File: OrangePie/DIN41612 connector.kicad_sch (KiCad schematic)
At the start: 0 parts

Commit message: Update rest of schematic
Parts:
- added J3: 09031967921, Connector_DIN:DIN41612_R_3x32_Female_Horizontal_THT, symbol DIN41612_3x32:09031967921
- added U10: IP4234CZ6,115, Package_TO_SOT_SMD:SC-74-6_1.55x2.9mm_P0.95mm, symbol Power_Protection:IP4234CZ6
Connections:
- new net 12V out: J3.a11, J3.a12, J3.b11, J3.b12, J3.c11, J3.c12
- new net 24v: J3.a14, J3.b14, J3.c14
- new net CAN1.+: J3.a5
- new net CAN1.-: J3.a6
- new net CAN1..+: J3.b5, J3.c5
- new net CAN1..-: J3.b6, J3.c6
- new net CAN2.+: J3.a8
- new net CAN2.-: J3.a9
- new net CAN2..+: J3.b8, J3.c8
- new net CAN2..-: J3.b9, J3.c9
- new net GND: J3.a1, J3.a10, J3.a13, J3.a15, J3.a32, J3.a4, J3.a7, J3.b1, J3.b10, J3.b13, J3.b15, J3.b2, J3.b32, J3.b4, J3.b7, J3.c1, J3.c10, J3.c13, J3.c15, J3.c32, J3.c4, J3.c7, U10.2 (VN)
- new net GPIOC0: J3.b16
- new net GPIOC1: J3.b17
- new net GPIOC10: J3.b26
- new net GPIOC11: J3.b27
- new net GPIOC12: J3.b28
- new net GPIOC13: J3.b29
- new net GPIOC14: J3.b30
- new net GPIOC15: J3.b31
- new net GPIOC2: J3.b18
- new net GPIOC3: J3.b19
- new net GPIOC4: J3.b20
- new net GPIOC5: J3.b21
- new net GPIOC6: J3.b22
- new net GPIOC7: J3.b23
- new net GPIOC8: J3.b24
- new net GPIOC9: J3.b25
- new net GPIOL0: J3.a16
- new net GPIOL1: J3.a17
- new net GPIOL10: J3.a26
- new net GPIOL11: J3.a27
- new net GPIOL12: J3.a28
- new net GPIOL13: J3.a29
- new net GPIOL14: J3.a30
- new net GPIOL15: J3.a31
- new net GPIOL2: J3.a18
- new net GPIOL3: J3.a19
- new net GPIOL4: J3.a20
- new net GPIOL5: J3.a21
- new net GPIOL6: J3.a22
- new net GPIOL7: J3.a23
- new net GPIOL8: J3.a24
- new net GPIOL9: J3.a25
- new net GPIOR0: J3.c16
- new net GPIOR1: J3.c17
- new net GPIOR10: J3.c26
- new net GPIOR11: J3.c27
- new net GPIOR12: J3.c28
- new net GPIOR13: J3.c29
- new net GPIOR14: J3.c30
- new net GPIOR15: J3.c31
- new net GPIOR2: J3.c18
- new net GPIOR3: J3.c19
- new net GPIOR4: J3.c20
- new net GPIOR5: J3.c21
- new net GPIOR6: J3.c22
- new net GPIOR7: J3.c23
- new net GPIOR8: J3.c24
- new net GPIOR9: J3.c25
- new net STDBY OUT: J3.a3, J3.b3, J3.c3
- new net USB1U.D+: J3.a2, U10.4, U10.6
- new net USB1U.D-: J3.c2, U10.1, U10.3
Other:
- note added: "USB"

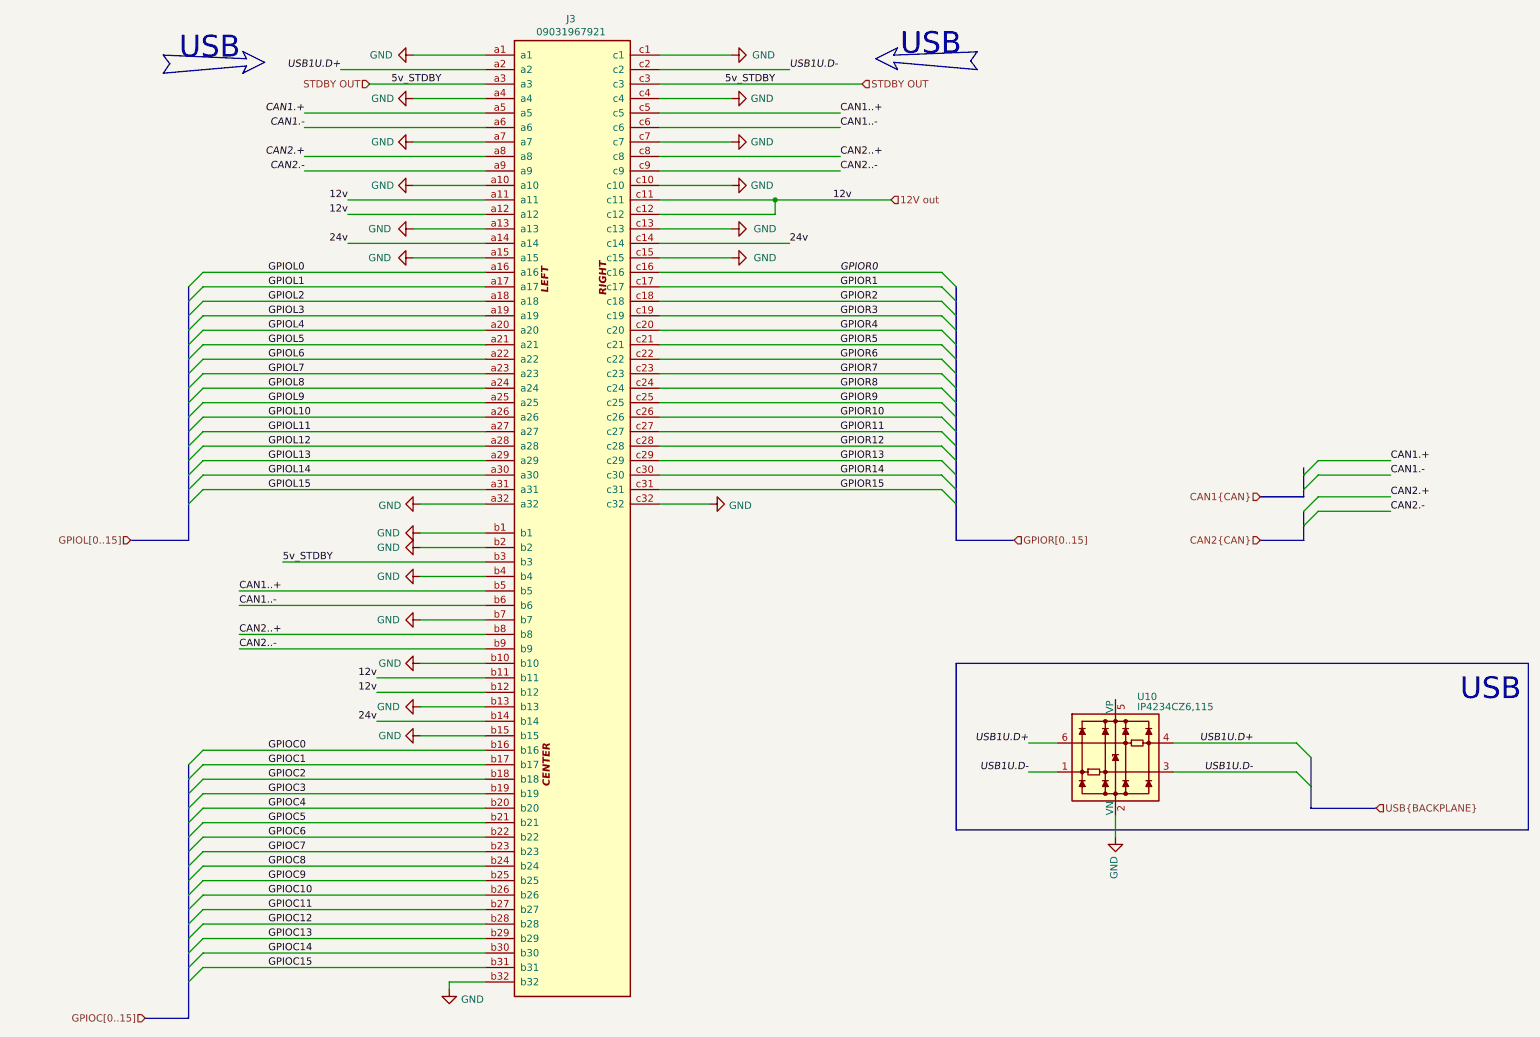
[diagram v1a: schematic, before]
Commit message: Add CH340 debug
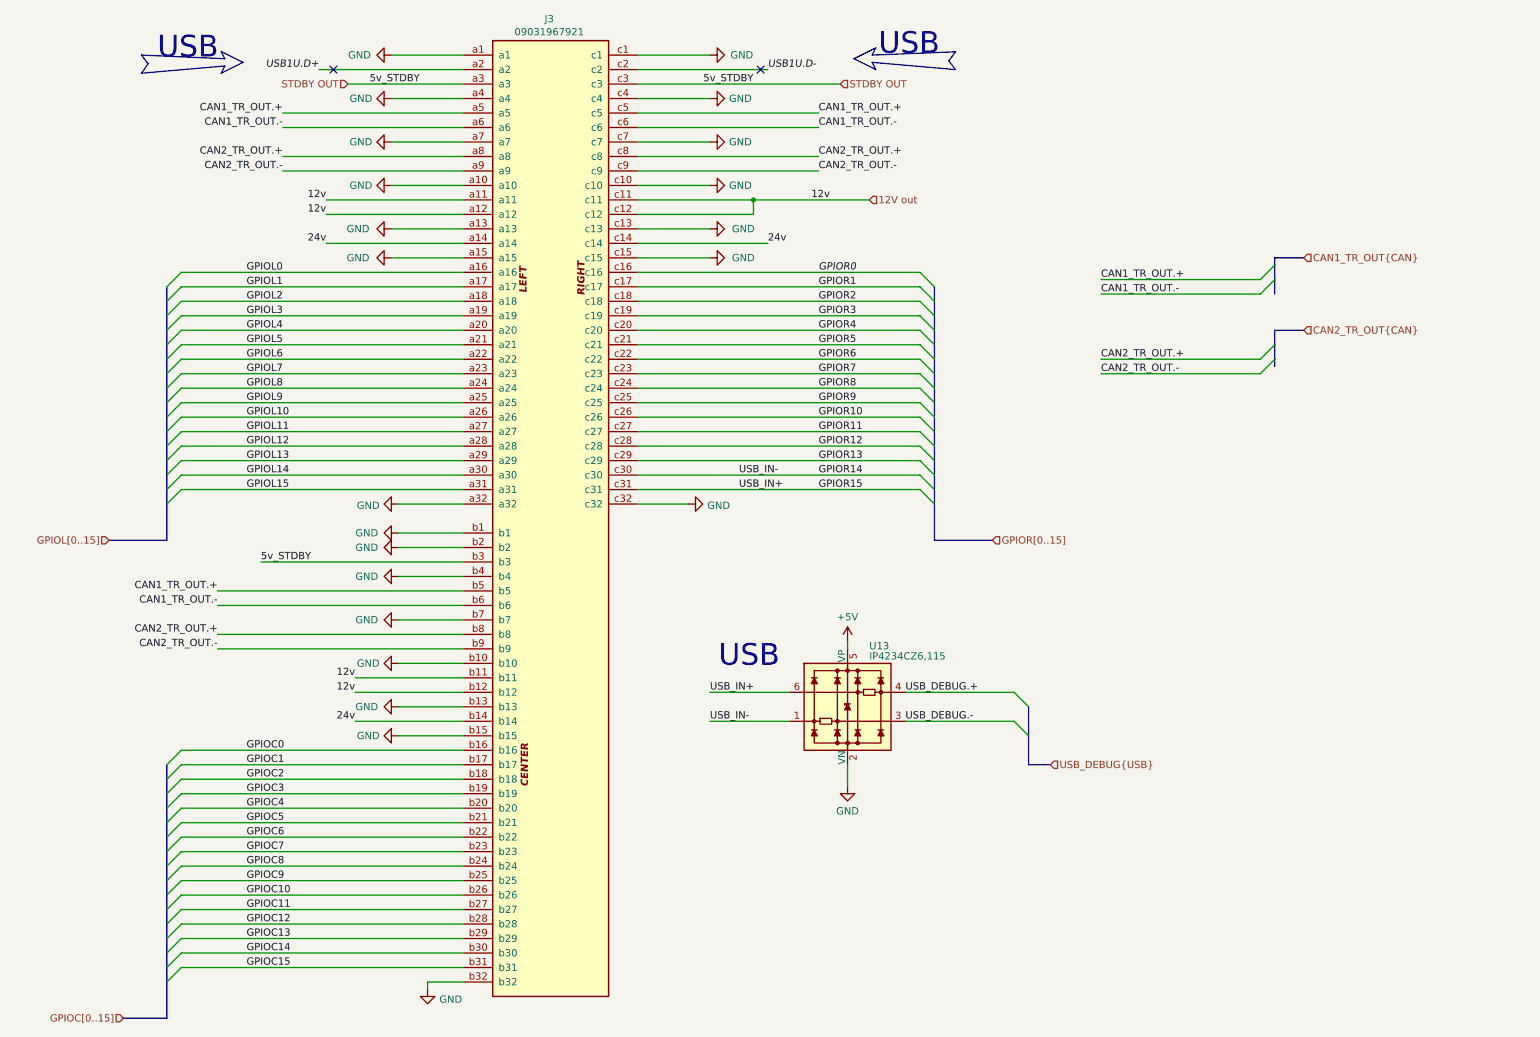
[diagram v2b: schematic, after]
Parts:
- removed U10: IP4234CZ6,115, Package_TO_SOT_SMD:SC-74-6_1.55x2.9mm_P0.95mm, symbol Power_Protection:IP4234CZ6
- added U13: IP4234CZ6,115, Package_TO_SOT_SMD:SC-74-6_1.55x2.9mm_P0.95mm, symbol Power_Protection:IP4234CZ6
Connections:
- net CAN1..+ is gone; now on net CAN1_TR_OUT.+: J3.b5, J3.c5
- net CAN1..- is gone; now on net CAN1_TR_OUT.-: J3.b6, J3.c6
- net CAN2..+ is gone; now on net CAN2_TR_OUT.+: J3.b8, J3.c8
- net CAN2..- is gone; now on net CAN2_TR_OUT.-: J3.b9, J3.c9
- net GND: now also U13.2 (VN)
- net GPIOR14: now also U13.1
- net GPIOR15: now also U13.6
- net CAN1.+ renamed CAN1_TR_OUT.+
- net CAN1.- renamed CAN1_TR_OUT.-
- net CAN2.+ renamed CAN2_TR_OUT.+
- net CAN2.- renamed CAN2_TR_OUT.-
- new net +5V: U13.5 (VP)
- new net USB_DEBUG.+: U13.4
- new net USB_DEBUG.-: U13.3
- no-connect marks 0 -> 2
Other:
- company: (none) -> ModuCard System
- moved on the sheet: J3
